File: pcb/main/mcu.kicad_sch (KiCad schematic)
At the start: 27 parts, among them J102 Conn_01x06, J103 Conn_02x13_Counter_Clockwise, J151 UART, J152 JTAG, SW151 Boot, SW152 Reset, U151 74LVC1G17, U152 74LVC1G17, U153 ESP32-S3-WROOM-1

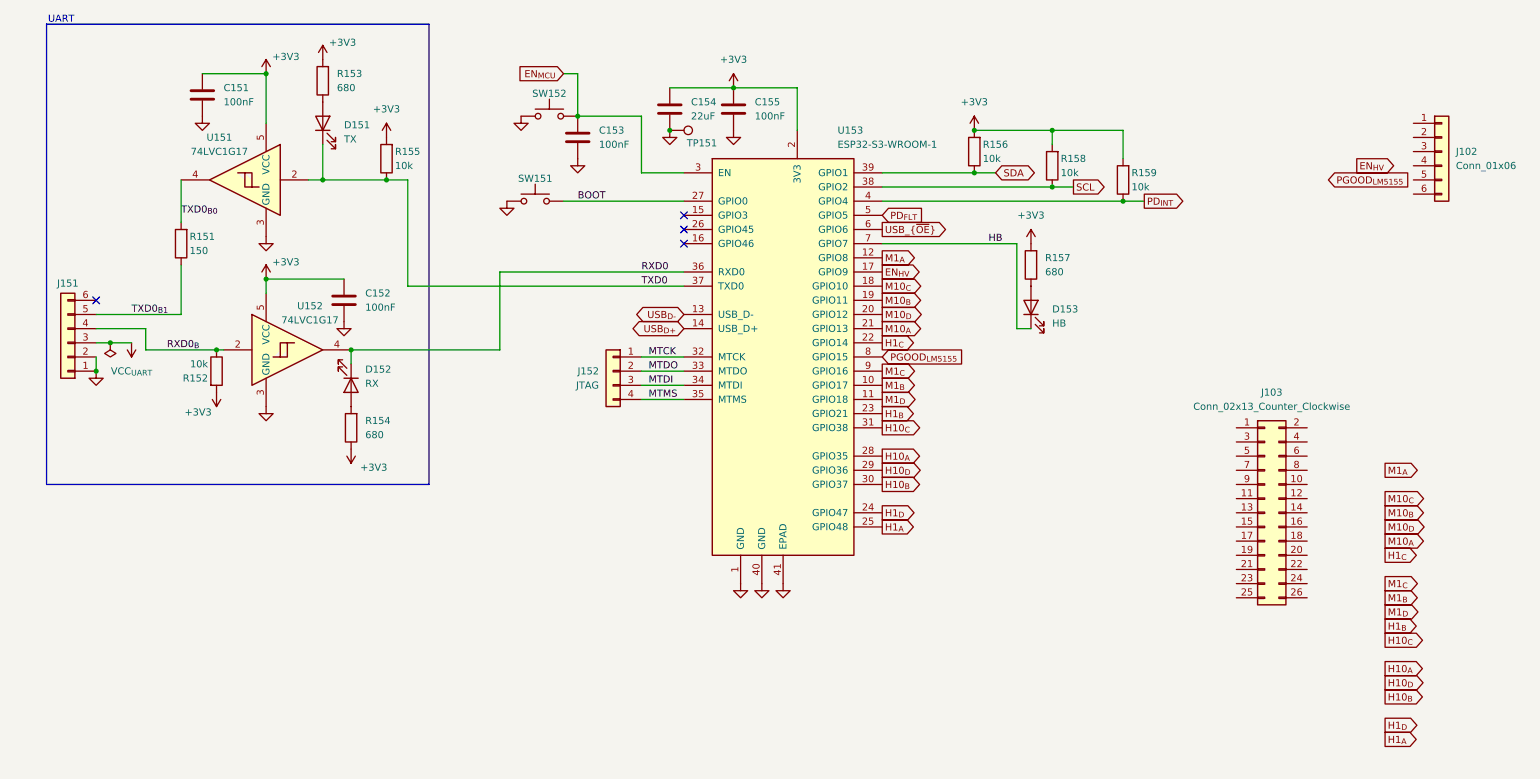
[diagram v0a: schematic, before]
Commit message: Split project into 3
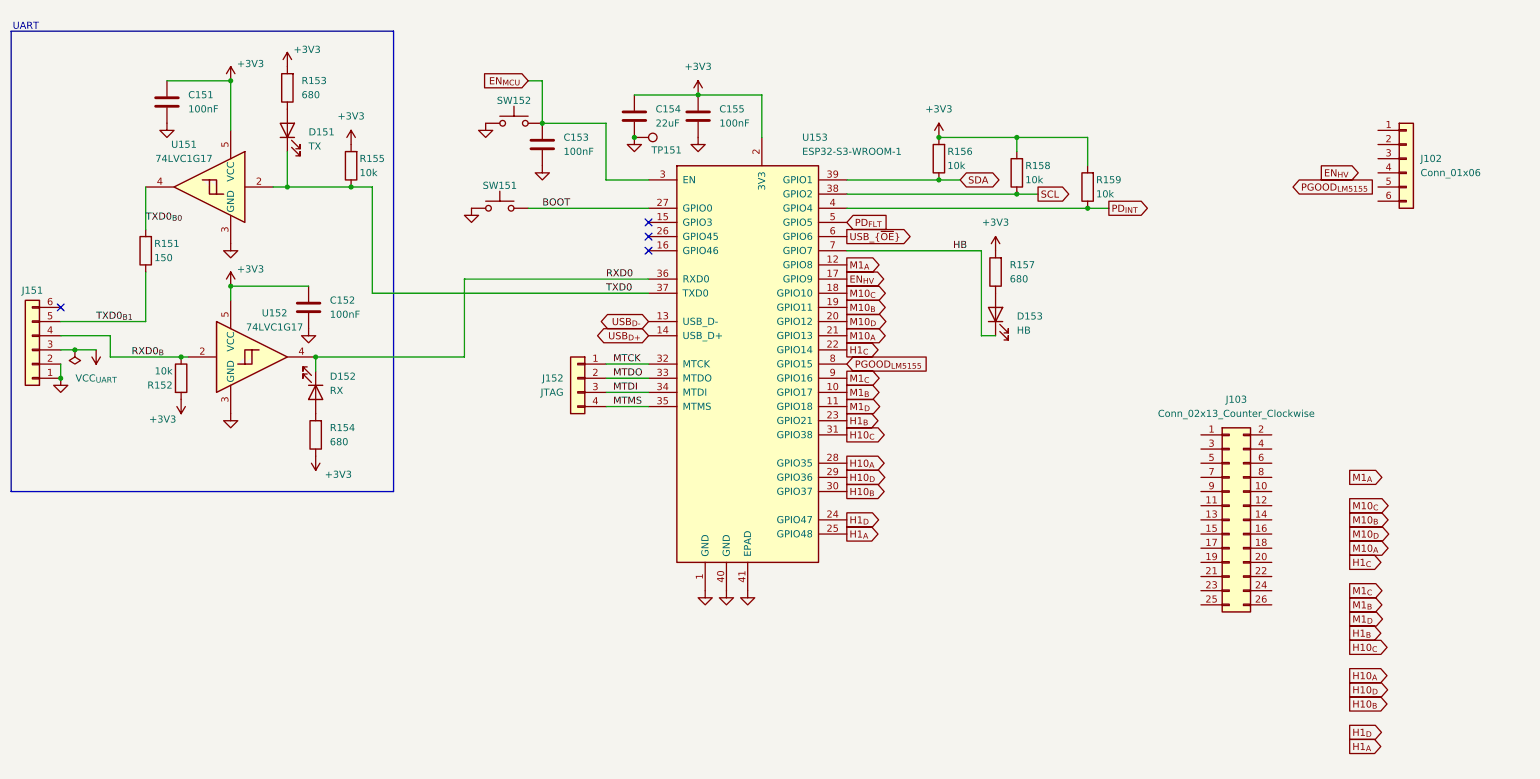
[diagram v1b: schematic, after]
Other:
- title: ${TITLE} -> (none)
- moved on the sheet: C151, C152, C153, C154, C155, D151, D152, D153, J102, J103, J151, J152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

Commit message: Rev B RC1
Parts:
- removed J152: JTAG, Connector_PinHeader_2.54mm:PinHeader_1x04_P2.54mm_Vertical, symbol Connector_Generic:Conn_01x04
- added J2: JTAG, nixie_clock:Samtec_FTSH-105-01-L-DV-K_2x05_P1.27mm_Vertical_SMD, symbol Connector_Generic:Conn_02x05_Odd_Even
- added J3: JTAG SRC, Connector_PinHeader_2.54mm:PinHeader_1x02_P2.54mm_Vertical, symbol Connector_Generic:Conn_01x02
- added R6: 100k, Resistor_SMD:R_0402_1005Metric, symbol Device:R
- added R7: 10k, Resistor_SMD:R_0402_1005Metric, symbol Device:R
- D3: renamed from D153; value HB -> STATUS
- J4: renamed from J103; value Conn_02x13_Counter_Clockwise -> 26 pin IDC
- renumbered C151 to C1, C152 to C2, C153 to C3, C154 to C4, C155 to C5, D151 to D1, D152 to D2, J151 to J1, J102 to J5, R151 to R1, R159 to R10, R158 to R11, R152 to R2, R153 to R3, R154 to R4, R155 to R5, R157 to R8, R156 to R9, SW151 to SW1, SW152 to SW2, TP151 to TP1, U151 to U1, U152 to U2, U153 to U3
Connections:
- net +3V3: now also J5.1 (Pin_1), J2.1 (Pin_1), R6.2
- net EN_{HV}: now also J5.2 (Pin_2), U3.12 (GPIO8); no longer U3.17 (GPIO9)
- net EN_{MCU}: now also J2.10 (Pin_10)
- net GND: now also J4.11 (Pin_11), J4.13 (Pin_13), J4.15 (Pin_15), J5.6 (Pin_6), J2.3 (Pin_3), J2.5 (Pin_5), J2.9 (Pin_9), J3.1 (Pin_1)
- net H10_{A}: now also J4.23 (Pin_23), U3.21 (GPIO13); no longer U3.28 (GPIO35)
- net H10_{B}: now also J4.24 (Pin_24), U3.22 (GPIO14); no longer U3.30 (GPIO37)
- net H10_{C}: now also J4.26 (Pin_26), U3.24 (GPIO47); no longer U3.31 (GPIO38)
- net H10_{D}: now also J4.25 (Pin_25), U3.23 (GPIO21); no longer U3.29 (GPIO36)
- net H1_{A}: now also J4.21 (Pin_21), U3.19 (GPIO11); no longer U3.25 (GPIO48)
- net H1_{B}: now also J4.19 (Pin_19), U3.17 (GPIO9); no longer U3.23 (GPIO21)
- net H1_{C}: now also J4.20 (Pin_20), U3.18 (GPIO10); no longer U3.22 (GPIO14)
- net H1_{D}: now also J4.22 (Pin_22), U3.20 (GPIO12); no longer U3.24 (GPIO47)
- net HB: now also U3.31 (GPIO38); no longer U3.7 (GPIO7)
- net M10_{A}: now also J4.8 (Pin_8), U3.11 (GPIO18); no longer U3.21 (GPIO13)
- net M10_{B}: now also J4.6 (Pin_6), U3.9 (GPIO16); no longer U3.19 (GPIO11)
- net M10_{C}: now also J4.5 (Pin_5), U3.8 (GPIO15); no longer U3.18 (GPIO10)
- net M10_{D}: now also J4.7 (Pin_7), U3.10 (GPIO17); no longer U3.20 (GPIO12)
- net M1_{A}: now also J4.2 (Pin_2), U3.5 (GPIO5); no longer U3.12 (GPIO8)
- net M1_{B}: now also J4.1 (Pin_1), U3.4 (GPIO4); no longer U3.10 (GPIO17)
- net M1_{C}: now also J4.3 (Pin_3), U3.6 (GPIO6); no longer U3.9 (GPIO16)
- net M1_{D}: now also J4.4 (Pin_4), U3.7 (GPIO7); no longer U3.11 (GPIO18)
- net MTCK: now also J2.4 (Pin_4)
- net MTDI: now also J2.8 (Pin_8)
- net MTDO: now also J2.6 (Pin_6)
- net MTMS: now also J2.2 (Pin_2)
- net PD_{FLT}: now also U3.30 (GPIO37); no longer U3.5 (GPIO5)
- net PD_{INT}: now also U3.28 (GPIO35); no longer U3.4 (GPIO4)
- net PGOOD_{LM5155}: now also J5.5 (Pin_5), U3.25 (GPIO48); no longer U3.8 (GPIO15)
- net USB_{~{OE}}: now also U3.29 (GPIO36); no longer U3.6 (GPIO6)
- net V_{BUS}: now reaches J5.3 (Pin_3)
- net V_{BUS}: now also J5.4 (Pin_4)
- net +5V: now reaches J4.12 (Pin_12)
- net +5V: now also J4.14 (Pin_14), J4.16 (Pin_16)
- net GPIO3: now reaches U3.15 (GPIO3)
- net GPIO3: now also R6.1, R7.2
- new net: J3.2 (Pin_2), R7.1
- no-connect marks 4 -> 8
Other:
- moved on the sheet: D3, R10, R8

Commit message: Rev B RC2
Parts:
- added R12: 10k, Resistor_SMD:R_0402_1005Metric, symbol Device:R
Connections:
- net +3V3: now also R12.2
- net BOOT: now also R12.1
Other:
- moved on the sheet: SW1
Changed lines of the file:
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@@
 	)
 	(junction
+		(at 101.6 50.8)
+		(diameter 0)
+		(color 0 0 0 0)
+	)
+	(junction
 		(at 39.37 137.16)
 		(diameter 0)
@@
 	(wire
 		(pts
-			(xy 109.22 50.8) (xy 130.81 50.8)
+			(xy 101.6 50.8) (xy 130.81 50.8)
 		)
 		(stroke
@@
 	(wire
 		(pts
+			(xy 92.71 41.91) (xy 101.6 41.91)
+		)
+		(stroke
+			(width 0)
+			(type default)
+		)
+	)
+	(wire
+		(pts
 			(xy 261.62 44.45) (xy 248.92 44.45)
 		)
@@
 	(wire
 		(pts
+			(xy 101.6 41.91) (xy 101.6 50.8)
+		)
+		(stroke
+			(width 0)
+			(type default)
+		)
+	)
+	(wire
+		(pts
 			(xy 66.04 46.99) (xy 77.47 46.99)
 		)
@@
 	(symbol
 		(lib_id "Switch:SW_Push")
-		(at 104.14 50.8 0)
+		(at 96.52 50.8 0)
 		(unit 1)
 		(exclude_from_sim no)
@@
 		(dnp no)
 		(property "Reference" "SW1"
-			(at 104.14 46.736 0)
+			(at 96.52 46.736 0)
 			(effects
 				(font
@@
 		)
 		(property "Value" "Boot"
-			(at 104.14 45.72 0)
+			(at 96.52 45.72 0)
 			(effects
 				(font
@@
 		)
 		(property "Footprint" "nixie_clock:SW_Panasonic_EVQ_4.9x4.9mm"
-			(at 104.14 45.72 0)
+			(at 96.52 45.72 0)
 			(effects
 				(font
@@
 		)
 		(property "Datasheet" "~"
-			(at 104.14 45.72 0)
+			(at 96.52 45.72 0)
 			(effects
 				(font
@@
 		)
 		(property "Description" "Push button switch, generic, two pins"
-			(at 104.14 50.8 0)
+			(at 96.52 50.8 0)
 			(effects
 				(font
@@
 		)
 		(property "MFG Part No" "EVQ-PT9A15"
-			(at 104.14 50.8 0)
+			(at 96.52 50.8 0)
 			(effects
 				(font
@@
 		)
 		(property "LCSC" ""
-			(at 104.14 50.8 0)
+			(at 96.52 50.8 0)
 			(effects
 				(font
@@
 	)
 	(symbol
+		(lib_id "Device:R")
+		(at 92.71 38.1 180)
+		(unit 1)
+		(exclude_from_sim no)
+		(in_bom yes)
+		(on_board yes)
+		(dnp no)
+		(property "Reference" "R12"
+			(at 94.234 36.83 0)
+			(effects
+				(font
+					(size 1.27 1.27)
+				)
+				(justify right)
+			)
+		)
+		(property "Value" "10k"
+			(at 94.234 39.37 0)
+			(effects
+				(font
+					(size 1.27 1.27)
+				)
+				(justify right)
+			)
+		)
+		(property "Footprint" "Resistor_SMD:R_0402_1005Metric"
+			(at 94.488 38.1 90)
+			(effects
+				(font
+					(size 1.27 1.27)
+				)
+				(hide yes)
+			)
+		)
+		(property "Datasheet" "~"
+			(at 92.71 38.1 0)
+			(effects
+				(font
+					(size 1.27 1.27)
+				)
+				(hide yes)
+			)
+		)
+		(property "Description" "Resistor"
+			(at 92.71 38.1 0)
+			(effects
+				(font
+					(size 1.27 1.27)
+				)
+				(hide yes)
+			)
+		)
+		(property "MFG Part No" "0402WGF1002TCE"
+			(at 92.71 38.1 0)
+			(effects
+				(font
+					(size 1.27 1.27)
+				)
+				(hide yes)
+			)
+		)
+		(property "LCSC" "C25744"
+			(at 92.71 38.1 0)
+			(effects
+				(font
+					(size 1.27 1.27)
+				)
+				(hide yes)
+			)
+		)
+		(pin "1"
+		)
+		(pin "2"
+		)
+		(instances
+			(project "main"
+				(path "/f225fc02-d36f-4469-bac4-82a576baae3a/0a78e122-cae8-43c8-ae5e-350b0dd676ce"
+					(reference "R12")
+					(unit 1)
+				)
+			)
+		)
+	)
+	(symbol
 		(lib_id "power:+5V")
 		(at 254 101.6 0)
@@
 	)
 	(symbol
+		(lib_id "power:+3V3")
+		(at 92.71 34.29 0)
+		(unit 1)
+		(exclude_from_sim no)
+		(in_bom yes)
+		(on_board yes)
+		(dnp no)
+		(fields_autoplaced yes)
+		(property "Reference" "#PWR03"
+			(at 92.71 38.1 0)
+			(effects
+				(font
+					(size 1.27 1.27)
+				)
+				(hide yes)
+			)
+		)
+		(property "Value" "+3V3"
+			(at 92.71 29.21 0)
+			(effects
+				(font
+					(size 1.27 1.27)
+				)
+			)
+		)
+		(property "Footprint" ""
+			(at 92.71 34.29 0)
+			(effects
+				(font
+					(size 1.27 1.27)
+				)
+				(hide yes)
+			)
+		)
+		(property "Datasheet" ""
+			(at 92.71 34.29 0)
+			(effects
+				(font
+					(size 1.27 1.27)
+				)
+				(hide yes)
+			)
+		)
+		(property "Description" "Power symbol creates a global label with name \"+3V3\""
+			(at 92.71 34.29 0)
+			(effects
+				(font
+					(size 1.27 1.27)
+				)
+				(hide yes)
+			)
+		)
+		(pin "1"
+		)
+		(instances
+			(project "main"
+				(path "/f225fc02-d36f-4469-bac4-82a576baae3a/0a78e122-cae8-43c8-ae5e-350b0dd676ce"
+					(reference "#PWR03")
+					(unit 1)
+				)
+			)
+		)
+	)
+	(symbol
 		(lib_id "74xGxx:74LVC1G17")
 		(at 60.96 77.47 0)
@@
 	(symbol
 		(lib_id "power:GND")
-		(at 99.06 50.8 0)
+		(at 91.44 50.8 0)
 		(unit 1)
 		(exclude_from_sim no)
@@
 		(fields_autoplaced yes)
 		(property "Reference" "#PWR0509"
-			(at 99.06 57.15 0)
+			(at 91.44 57.15 0)
 			(effects
 				(font
@@
 		)
 		(property "Value" "GND"
-			(at 99.06 55.88 0)
+			(at 91.44 55.88 0)
 			(effects
 				(font
@@
 		)
 		(property "Footprint" ""
-			(at 99.06 50.8 0)
+			(at 91.44 50.8 0)
 			(effects
 				(font
@@
 		)
 		(property "Datasheet" ""
-			(at 99.06 50.8 0)
+			(at 91.44 50.8 0)
 			(effects
 				(font
@@
 		)
 		(property "Description" "Power symbol creates a global label with name \"GND\" , ground"
-			(at 99.06 50.8 0)
+			(at 91.44 50.8 0)
 			(effects
 				(font
@@
 		)
 		(property "MFG Part No" ""
-			(at 99.06 50.8 0)
+			(at 91.44 50.8 0)
 			(effects
 				(font
@@
 		)
 		(property "LCSC" ""
-			(at 99.06 50.8 0)
+			(at 91.44 50.8 0)
 			(effects
 				(font

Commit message: Final Rev B
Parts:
- J2, J3, J4, J5: now left out of the parts list
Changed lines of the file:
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@@
 		(unit 1)
 		(exclude_from_sim no)
-		(in_bom yes)
+		(in_bom no)
 		(on_board yes)
 		(dnp no)
@@
 		(unit 1)
 		(exclude_from_sim no)
-		(in_bom yes)
+		(in_bom no)
 		(on_board yes)
 		(dnp no)
@@
 		(unit 1)
 		(exclude_from_sim no)
-		(in_bom yes)
+		(in_bom no)
 		(on_board yes)
 		(dnp no)
@@
 		(unit 1)
 		(exclude_from_sim no)
-		(in_bom yes)
+		(in_bom no)
 		(on_board yes)
 		(dnp no)

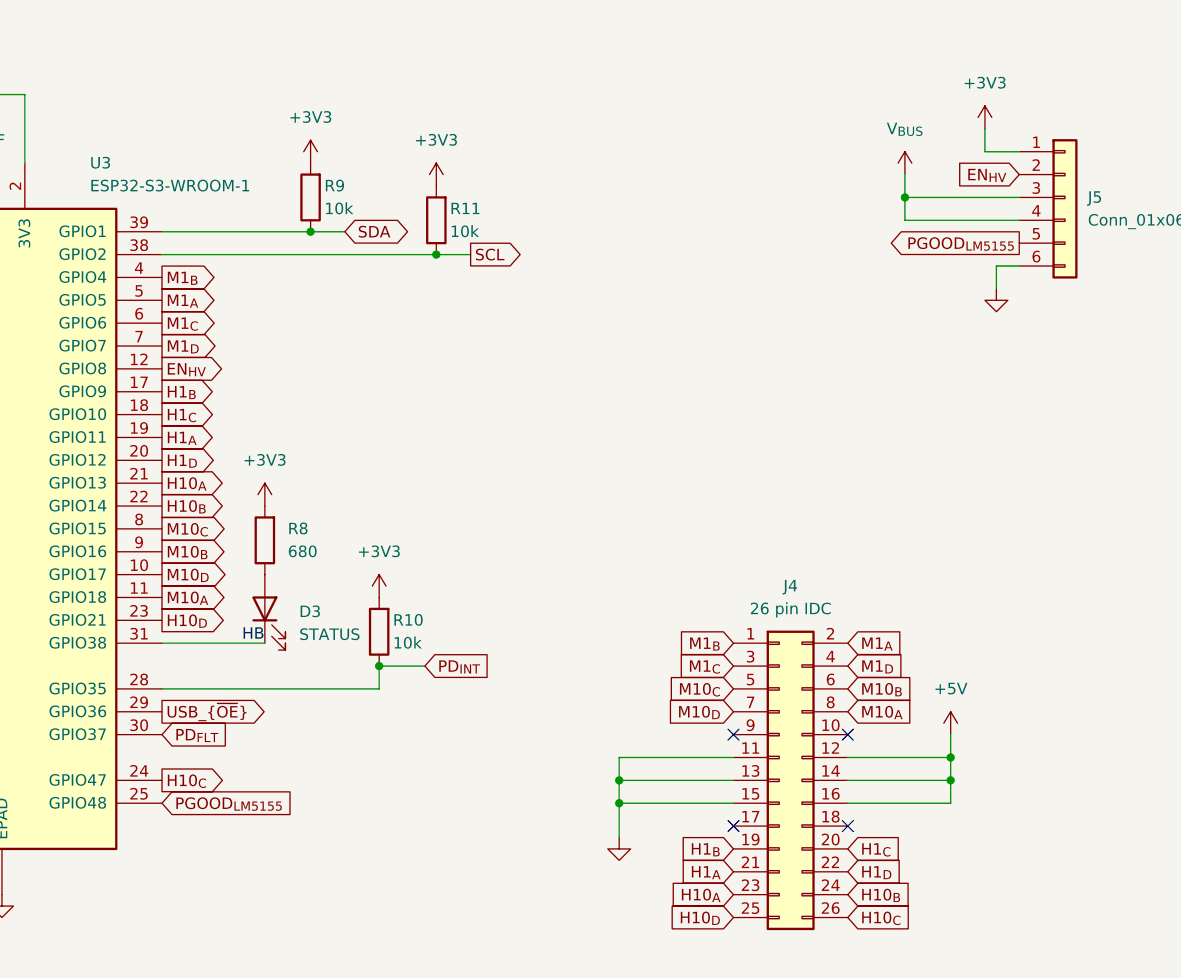
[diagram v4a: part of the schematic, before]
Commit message: HV converter Rev C redesign around LM5156
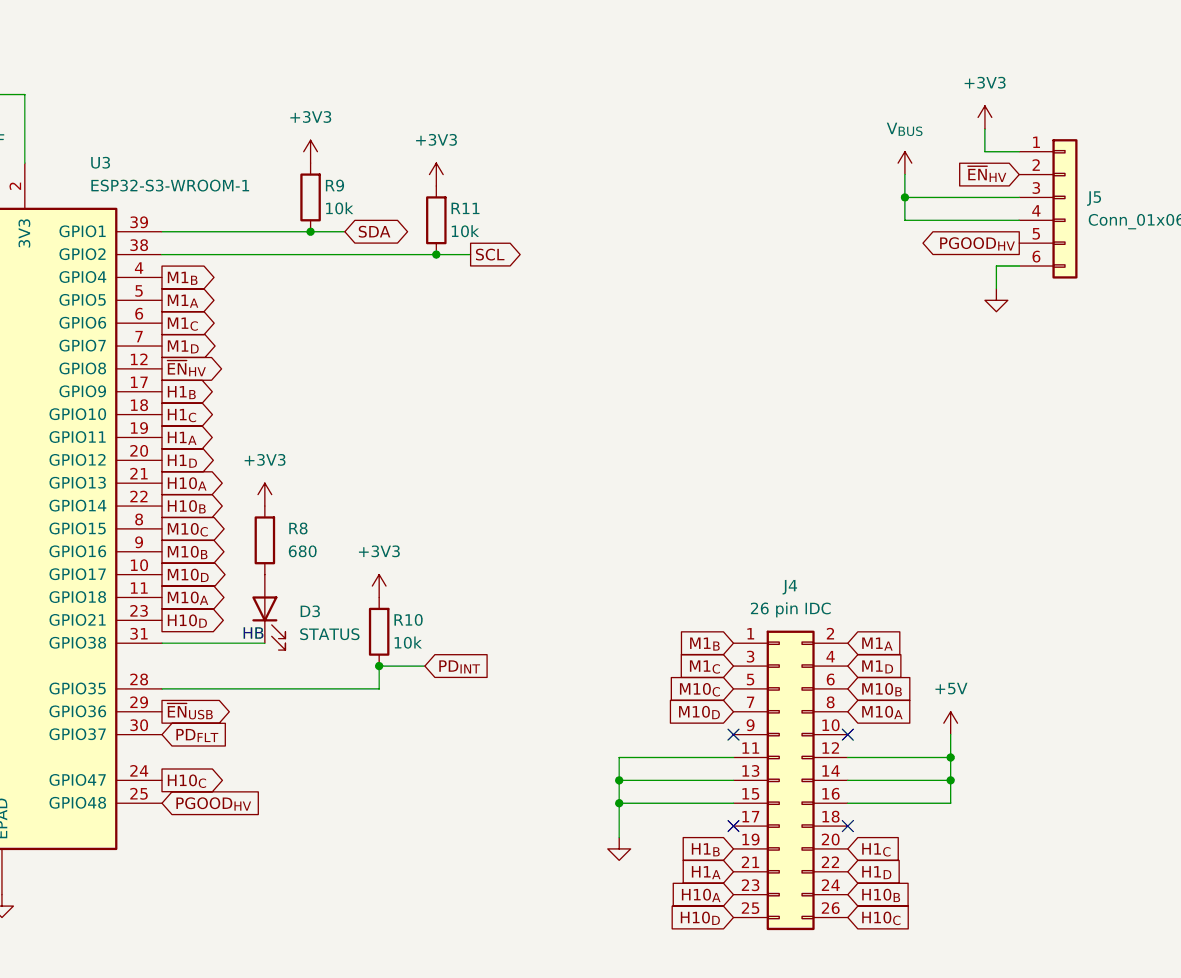
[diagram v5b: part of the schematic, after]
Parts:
- J2: footprint nixie_clock:Samtec_FTSH-105-01-L-DV-K_2x05_P1.27mm_Vertical_SMD -> 0_nixie_clock:Samtec_FTSH-105-01-L-DV-K_2x05_P1.27mm_Vertical_SMD
- SW1, SW2: footprint nixie_clock:SW_Panasonic_EVQ_4.9x4.9mm -> 0_nixie_clock:SW_Panasonic_EVQ_4.9x4.9mm
- U3: footprint nixie_clock:ESP32-S3-WROOM-1 -> 0_nixie_clock:ESP32-S3-WROOM-1; symbol nixie_clock:ESP32-S3-WROOM-1 -> 0_nixie_clock:ESP32-S3-WROOM-1
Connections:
- net EN_{HV} renamed ~{EN}_{HV}
- net PGOOD_{LM5155} renamed PGOOD_{HV}
- net USB_{~{OE}} renamed ~{EN}_{USB}

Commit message: Clock Face Rev C
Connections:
- net H10_{A}: now also J4.19 (Pin_19); no longer J4.23 (Pin_23)
- net H10_{B}: now also J4.23 (Pin_23); no longer J4.24 (Pin_24)
- net H10_{C}: now also J4.25 (Pin_25); no longer J4.26 (Pin_26)
- net H10_{D}: now also J4.21 (Pin_21); no longer J4.25 (Pin_25)
- net H1_{A}: now also J4.26 (Pin_26); no longer J4.21 (Pin_21)
- net H1_{B}: now also J4.22 (Pin_22); no longer J4.19 (Pin_19)
- net H1_{D}: now also J4.24 (Pin_24); no longer J4.22 (Pin_22)
- net M10_{B}: now also J4.4 (Pin_4); no longer J4.6 (Pin_6)
- net M10_{C}: now also J4.2 (Pin_2); no longer J4.5 (Pin_5)
- net M10_{D}: now also J4.6 (Pin_6); no longer J4.7 (Pin_7)
- net M1_{A}: now also J4.1 (Pin_1); no longer J4.2 (Pin_2)
- net M1_{B}: now also J4.5 (Pin_5); no longer J4.1 (Pin_1)
- net M1_{C}: now also J4.7 (Pin_7); no longer J4.3 (Pin_3)
- net M1_{D}: now also J4.3 (Pin_3); no longer J4.4 (Pin_4)

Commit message: Main board Rev C
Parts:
- added J131: I2C, Connector_PinHeader_2.54mm:PinHeader_1x04_P2.54mm_Vertical, symbol Connector_Generic:Conn_01x04
- J3: footprint Connector_PinHeader_2.54mm:PinHeader_1x02_P2.54mm_Vertical -> Connector_PinHeader_1.27mm:PinHeader_1x02_P1.27mm_Vertical; MFG Part No (none) -> M50-3530242; Note (none) -> Close with M50-1900005 or equivelent
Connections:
- net +3V3: now also J131.2 (Pin_2)
- net GND: now also J131.1 (Pin_1)
- net H10_{A}: now also U3.17 (GPIO9); no longer U3.21 (GPIO13)
- net H10_{B}: now also U3.21 (GPIO13); no longer U3.22 (GPIO14)
- net H10_{C}: now also U3.23 (GPIO21); no longer U3.24 (GPIO47)
- net H10_{D}: now also U3.19 (GPIO11); no longer U3.23 (GPIO21)
- net H1_{A}: now also U3.24 (GPIO47); no longer U3.19 (GPIO11)
- net H1_{B}: now also U3.20 (GPIO12); no longer U3.17 (GPIO9)
- net H1_{D}: now also U3.22 (GPIO14); no longer U3.20 (GPIO12)
- net M10_{B}: now also U3.7 (GPIO7); no longer U3.9 (GPIO16)
- net M10_{C}: now also U3.5 (GPIO5); no longer U3.8 (GPIO15)
- net M10_{D}: now also U3.9 (GPIO16); no longer U3.10 (GPIO17)
- net M1_{A}: now also U3.4 (GPIO4); no longer U3.5 (GPIO5)
- net M1_{B}: now also U3.8 (GPIO15); no longer U3.4 (GPIO4)
- net M1_{C}: now also U3.10 (GPIO17); no longer U3.6 (GPIO6)
- net M1_{D}: now also U3.6 (GPIO6); no longer U3.7 (GPIO7)
- net SCL: now also J131.4 (Pin_4)
- net SDA: now also J131.3 (Pin_3)
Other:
- note added: "I2C Breakout"
- note added: "JTAG"
- moved on the sheet: J2, J3, R6, R7
